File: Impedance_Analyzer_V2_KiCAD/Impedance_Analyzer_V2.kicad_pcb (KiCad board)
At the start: 2 copper layers, 94.4 x 90 mm, 87 parts, among them J1 Conn_Coaxial, J10 Conn_02x02_Counter_Clockwise, J11 Screw_Terminal_01x03, J12 Conn_02x02_Counter_Clockwise, J13 Conn_02x02_Counter_Clockwise, J14 Conn_02x02_Counter_Clockwise, J15 Conn_02x02_Counter_Clockwise, J16 Conn_02x02_Counter_Clockwise, J17 Conn_02x02_Counter_Clockwise, J2 Conn_Coaxial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

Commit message: Add STEP file, minor changes
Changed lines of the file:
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@@
     )
     (pad_to_mask_clearance 0)
-    (aux_axis_origin 70 142.5)
     (grid_origin 70 142.5)
     (pcbplotparams
@@
       (drillshape 0)
       (scaleselection 1)
-      (outputdirectory "Impedance Analyzer_V2RevA_Gerb/")
+      (outputdirectory "Impedance Analyzer_V2RevB_Gerb/")
     )
   )
@@
     (fp_line (start 1.6 -0.8) (end 1.6 0.8) (layer "F.Fab") (width 0.1))
     (fp_line (start 1.6 0.8) (end -1.6 0.8) (layer "F.Fab") (width 0.1))
-    (pad "1" smd roundrect locked (at -1.4625 0 180) (size 1.125 1.75) (layers "F.Cu" "F.Paste" "F.Mask") (roundrect_rratio 0.222222)
+    (pad "1" smd roundrect locked (at -1.4625 0 180) (size 1.125 1.75) (layers "F.Cu" "F.Paste" "F.Mask") (roundrect_rratio 0.2222222222)
       (net 57 "Net-(J17-Pad2)") (pintype "passive"))
-    (pad "2" smd roundrect locked (at 1.4625 0 180) (size 1.125 1.75) (layers "F.Cu" "F.Paste" "F.Mask") (roundrect_rratio 0.222222)
+    (pad "2" smd roundrect locked (at 1.4625 0 180) (size 1.125 1.75) (layers "F.Cu" "F.Paste" "F.Mask") (roundrect_rratio 0.2222222222)
       (net 8 "Net-(BUF1-Pad6)") (pintype "passive"))
     (model "${KICAD6_3DMODEL_DIR}/Resistor_SMD.3dshapes/R_1206_3216Metric.wrl"
@@
     (fp_line (start -1.6 0.8) (end -1.6 -0.8) (layer "F.Fab") (width 0.1))
     (fp_line (start 1.6 -0.8) (end 1.6 0.8) (layer "F.Fab") (width 0.1))
-    (pad "1" smd roundrect locked (at -1.4625 0) (size 1.125 1.75) (layers "F.Cu" "F.Paste" "F.Mask") (roundrect_rratio 0.222222)
+    (pad "1" smd roundrect locked (at -1.4625 0) (size 1.125 1.75) (layers "F.Cu" "F.Paste" "F.Mask") (roundrect_rratio 0.2222222222)
       (net 47 "Net-(R15-Pad1)") (pintype "passive"))
-    (pad "2" smd roundrect locked (at 1.4625 0) (size 1.125 1.75) (layers "F.Cu" "F.Paste" "F.Mask") (roundrect_rratio 0.222222)
+    (pad "2" smd roundrect locked (at 1.4625 0) (size 1.125 1.75) (layers "F.Cu" "F.Paste" "F.Mask") (roundrect_rratio 0.2222222222)
       (net 8 "Net-(BUF1-Pad6)") (pintype "passive"))
     (model "${KICAD6_3DMODEL_DIR}/Resistor_SMD.3dshapes/R_1206_3216Metric.wrl"
@@
     (fp_line (start -1.6 0.8) (end 1.6 0.8) (layer "B.Fab") (width 0.1))
     (fp_line (start 1.6 0.8) (end 1.6 -0.8) (layer "B.Fab") (width 0.1))
-    (pad "1" smd roundrect locked (at -1.5625 0 270) (size 1.325 1.8) (layers "B.Cu" "B.Paste" "B.Mask") (roundrect_rratio 0.188679)
+    (pad "1" smd roundrect locked (at -1.5625 0 270) (size 1.325 1.8) (layers "B.Cu" "B.Paste" "B.Mask") (roundrect_rratio 0.1886792453)
       (net 16 "+5VP") (pintype "passive"))
-    (pad "2" smd roundrect locked (at 1.5625 0 270) (size 1.325 1.8) (layers "B.Cu" "B.Paste" "B.Mask") (roundrect_rratio 0.188679)
+    (pad "2" smd roundrect locked (at 1.5625 0 270) (size 1.325 1.8) (layers "B.Cu" "B.Paste" "B.Mask") (roundrect_rratio 0.1886792453)
       (net 1 "GND") (pintype "passive"))
     (model "${KICAD6_3DMODEL_DIR}/Capacitor_SMD.3dshapes/C_1206_3216Metric.wrl"
@@
     (fp_line (start -1.6 0.8) (end 1.6 0.8) (layer "B.Fab") (width 0.1))
     (fp_line (start 1.6 0.8) (end 1.6 -0.8) (layer "B.Fab") (width 0.1))
-    (pad "1" smd roundrect locked (at -1.5625 0 270) (size 1.325 1.8) (layers "B.Cu" "B.Paste" "B.Mask") (roundrect_rratio 0.188679)
+    (pad "1" smd roundrect locked (at -1.5625 0 270) (size 1.325 1.8) (layers "B.Cu" "B.Paste" "B.Mask") (roundrect_rratio 0.1886792453)
       (net 1 "GND") (pintype "passive"))
-    (pad "2" smd roundrect locked (at 1.5625 0 270) (size 1.325 1.8) (layers "B.Cu" "B.Paste" "B.Mask") (roundrect_rratio 0.188679)
+    (pad "2" smd roundrect locked (at 1.5625 0 270) (size 1.325 1.8) (layers "B.Cu" "B.Paste" "B.Mask") (roundrect_rratio 0.1886792453)
       (net 15 "-5V") (pintype "passive"))
     (model "${KICAD6_3DMODEL_DIR}/Capacitor_SMD.3dshapes/C_1206_3216Metric.wrl"
@@
     (fp_line (start -1.6 0.8) (end 1.6 0.8) (layer "B.Fab") (width 0.1))
     (fp_line (start 1.6 0.8) (end 1.6 -0.8) (layer "B.Fab") (width 0.1))
-    (pad "1" smd roundrect locked (at -1.5625 0) (size 1.325 1.8) (layers "B.Cu" "B.Paste" "B.Mask") (roundrect_rratio 0.188679)
+    (pad "1" smd roundrect locked (at -1.5625 0) (size 1.325 1.8) (layers "B.Cu" "B.Paste" "B.Mask") (roundrect_rratio 0.1886792453)
       (net 16 "+5VP") (pintype "passive"))
-    (pad "2" smd roundrect locked (at 1.5625 0) (size 1.325 1.8) (layers "B.Cu" "B.Paste" "B.Mask") (roundrect_rratio 0.188679)
+    (pad "2" smd roundrect locked (at 1.5625 0) (size 1.325 1.8) (layers "B.Cu" "B.Paste" "B.Mask") (roundrect_rratio 0.1886792453)
       (net 1 "GND") (pintype "passive"))
     (model "${KICAD6_3DMODEL_DIR}/Capacitor_SMD.3dshapes/C_1206_3216Metric.wrl"
@@
     (fp_line (start -1.6 -0.8) (end -1.6 0.8) (layer "B.Fab") (width 0.1))
     (fp_line (start 1.6 0.8) (end 1.6 -0.8) (layer "B.Fab") (width 0.1))
-    (pad "1" smd roundrect locked (at -1.5625 0) (size 1.325 1.8) (layers "B.Cu" "B.Paste" "B.Mask") (roundrect_rratio 0.188679)
+    (pad "1" smd roundrect locked (at -1.5625 0) (size 1.325 1.8) (layers "B.Cu" "B.Paste" "B.Mask") (roundrect_rratio 0.1886792453)
       (net 1 "GND") (pintype "passive"))
-    (pad "2" smd roundrect locked (at 1.5625 0) (size 1.325 1.8) (layers "B.Cu" "B.Paste" "B.Mask") (roundrect_rratio 0.188679)
+    (pad "2" smd roundrect locked (at 1.5625 0) (size 1.325 1.8) (layers "B.Cu" "B.Paste" "B.Mask") (roundrect_rratio 0.1886792453)
       (net 15 "-5V") (pintype "passive"))
     (model "${KICAD6_3DMODEL_DIR}/Capacitor_SMD.3dshapes/C_1206_3216Metric.wrl"

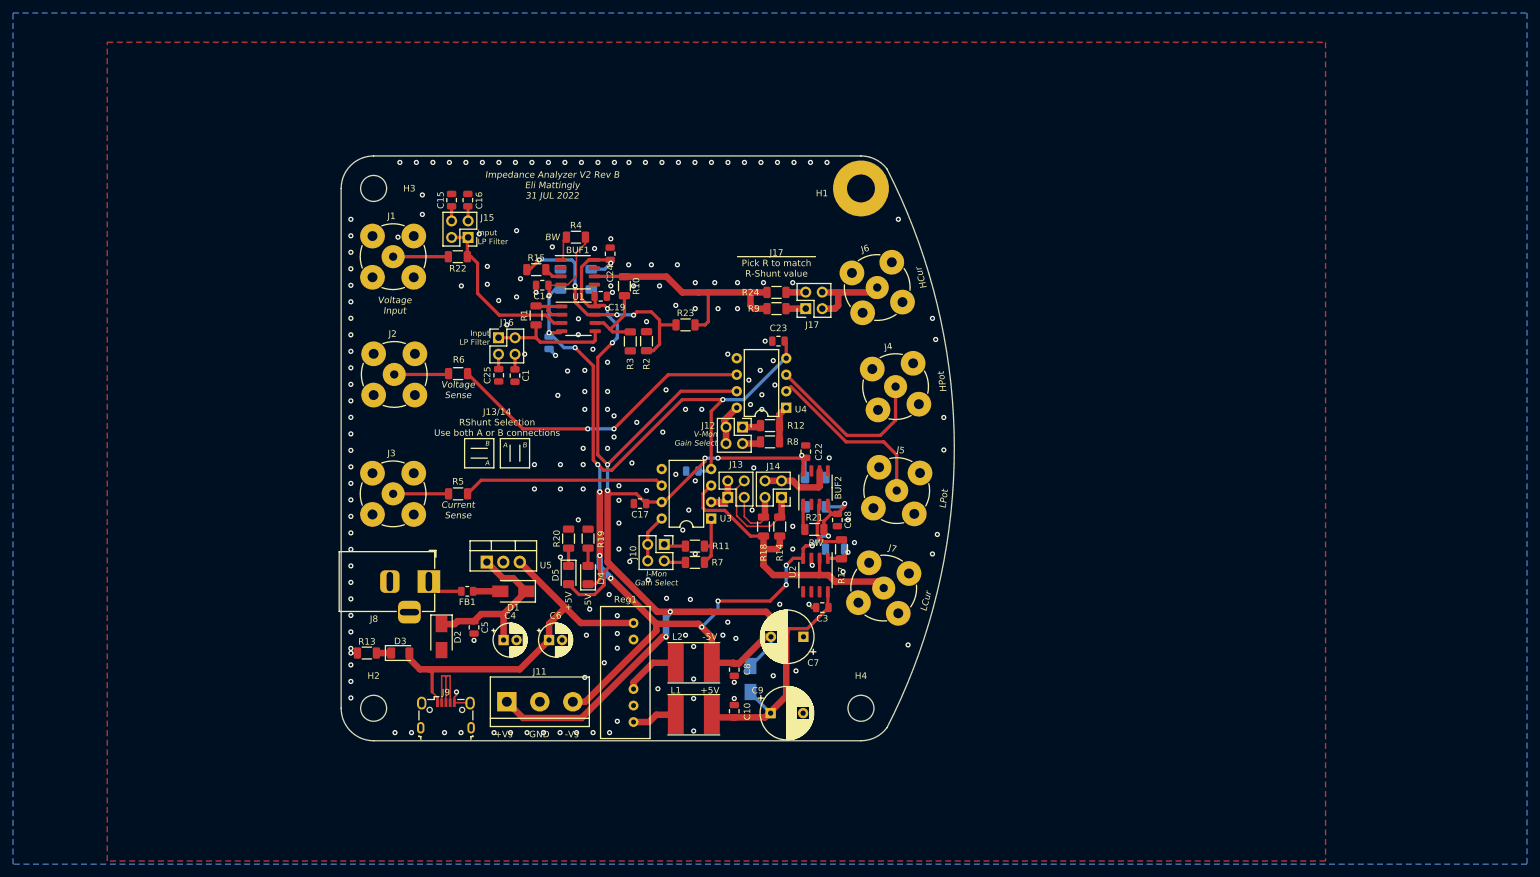
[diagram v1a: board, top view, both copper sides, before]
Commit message: Make Rev C + Curve tracer init
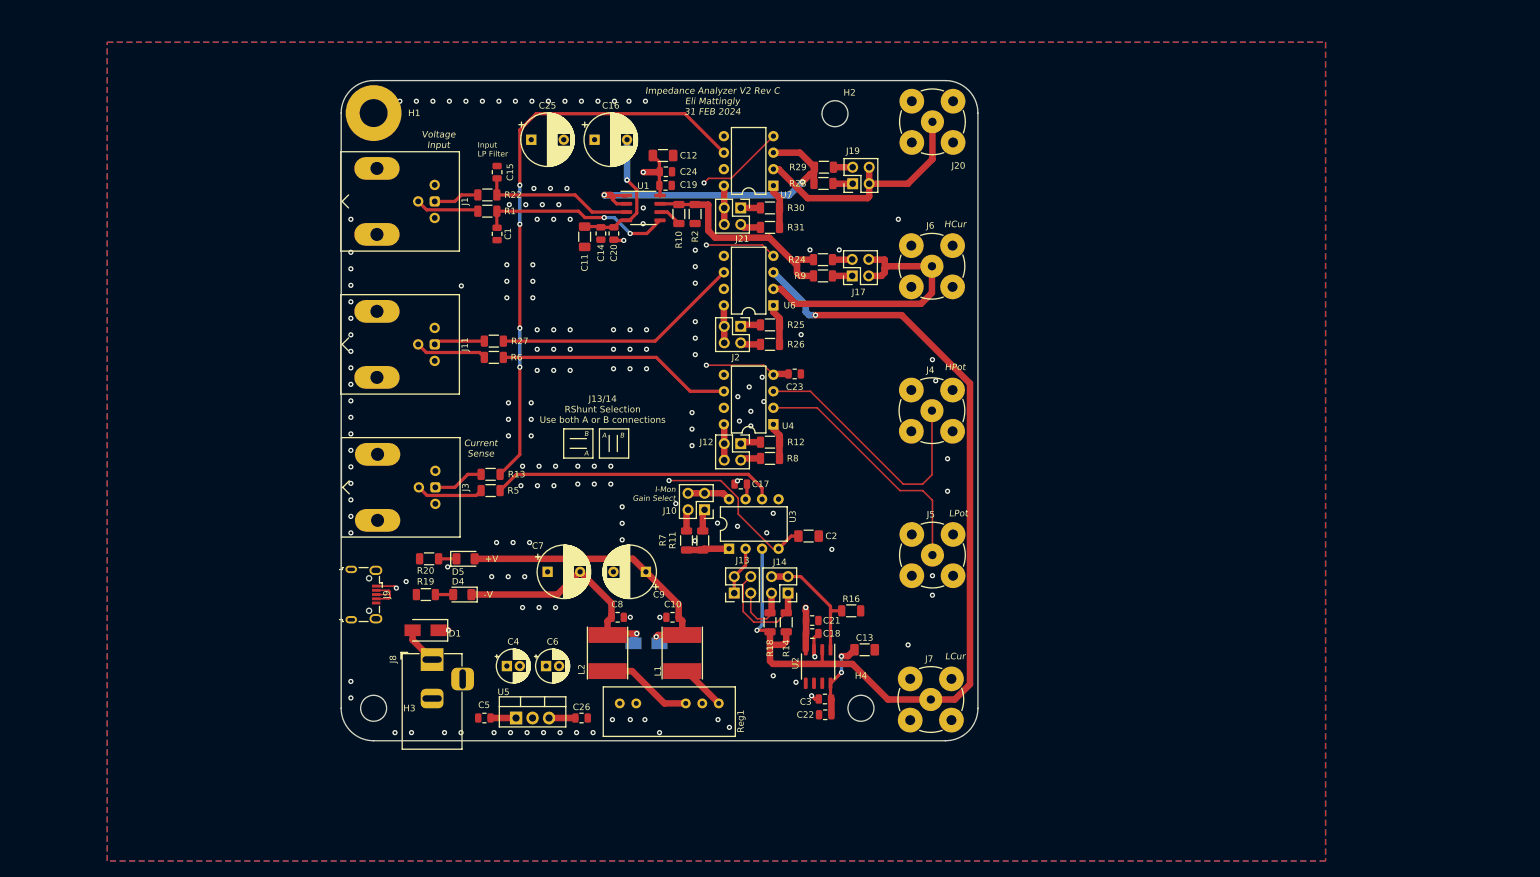
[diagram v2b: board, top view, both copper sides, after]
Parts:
- removed BUF1, BUF2: BUF634, Package_SO:SO-8_3.9x4.9mm_P1.27mm
- removed D2: D_TVS, Diode_SMD:D_SMA
- removed D3: LED, LED_SMD:LED_1206_3216Metric
- removed FB1: Ferrite_Bead, Resistor_SMD:R_0805_2012Metric
- removed J15, J16: Conn_02x02_Counter_Clockwise, Connector_PinHeader_2.54mm:PinHeader_2x02_P2.54mm_Vertical
- removed R15, R17: 50, Resistor_SMD:R_1206_3216Metric
- removed R21, R23, R3, R4: DNP, Resistor_SMD:R_1206_3216Metric
- added C26: 100n, Capacitor_SMD:C_0805_2012Metric, F.Cu at (107.0, 139.0)
- added J19: Conn_02x02_Counter_Clockwise, Connector_PinHeader_2.54mm:PinHeader_2x02_P2.54mm_Vertical, F.Cu at (148.7, 56.8)
- added J20: Conn_Coaxial, Connector_Coaxial:BNC_TEConnectivity_1478204_Vertical, F.Cu at (161.0, 47.2)
- added J21: Conn_02x02_Counter_Clockwise, Connector_PinHeader_2.54mm:PinHeader_2x02_P2.54mm_Vertical, F.Cu at (131.5, 60.5)
- added R25: 1k, Resistor_SMD:R_1206_3216Metric, F.Cu at (136.0, 78.5)
- added R26: 10k, Resistor_SMD:R_1206_3216Metric, F.Cu at (136.0, 81.5)
- added R27: 47, Resistor_SMD:R_1206_3216Metric, F.Cu at (93.5, 81.0)
- added R28: 1k, Resistor_SMD:R_1206_3216Metric, F.Cu at (144.2, 56.7)
- added R29: 10k, Resistor_SMD:R_1206_3216Metric, F.Cu at (144.3, 54.2)
- added R30: 1k, Resistor_SMD:R_1206_3216Metric, F.Cu at (136.0, 60.5)
- added R31: 10k, Resistor_SMD:R_1206_3216Metric, F.Cu at (136.0, 63.5)
- added U6: INA129, Package_DIP:DIP-8_W7.62mm, F.Cu at (136.5, 75.5)
- added U7: INA129, Package_DIP:DIP-8_W7.62mm, F.Cu at (136.5, 57.1)
- C11, C12, C13, C2, C20, C21, R16: moved to F.Cu
- C15: value 1n -> 10n
- C16, C25: value 10n -> CP; footprint Capacitor_SMD:C_0805_2012Metric -> Capacitor_THT:CP_Radial_D8.0mm_P5.00mm
- J1, J3: value Conn_Coaxial -> Conn_Coaxial_x2; footprint Connector_Coaxial:BNC_TEConnectivity_1478204_Vertical -> Connector_Coaxial:BNC_Win_364A2x95_Horizontal
- J11: value Screw_Terminal_01x03 -> Conn_Coaxial_x2; footprint TerminalBlock:TerminalBlock_bornier-3_P5.08mm -> Connector_Coaxial:BNC_Win_364A2x95_Horizontal
- J2: value Conn_Coaxial -> Conn_02x02_Counter_Clockwise; footprint Connector_Coaxial:BNC_TEConnectivity_1478204_Vertical -> Connector_PinHeader_2.54mm:PinHeader_2x02_P2.54mm_Vertical
- R13: value 1k -> 47
- U1, U2: value LM358 -> AD8022
- moved H2 115.8 mm to (146.0, 46.0)
- moved H3 80.0 mm to (75.0, 137.5)
- moved H1 75.9 mm to (75.0, 45.9)
- moved J11 56.1 mm to (84.4, 81.5), turned to 90 degrees
- moved J2 53.8 mm to (131.5, 78.7), turned to -90 degrees
- moved C7 40.6 mm to (101.8, 116.5), turned to 0 degrees
- moved C22 40.6 mm to (144.5, 138.5), turned to 180 degrees
- moved C25 36.6 mm to (99.3, 50.0), turned to 0 degrees
- moved R13 33.4 mm to (93.0, 101.5)
- moved C21 29.5 mm to (142.5, 124.0), turned to 0 degrees
- moved C9 29.0 mm to (116.9, 116.5), turned to 180 degrees
- moved C13 27.6 mm to (150.6, 128.5)
- moved R19 26.4 mm to (83.0, 120.0), turned to 180 degrees
- moved U5 24.4 mm to (96.9, 139.0)
- moved J9 22.4 mm to (73.5, 120.0), turned to -90 degrees
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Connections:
- C1 pad 1: Net-(C1-Pad1) -> Net-(R1-Pad1)
- C15 pad 1: Net-(C15-Pad1) -> Net-(R22-Pad1)
- C16 pad 1: Net-(C16-Pad1) -> GND
- C16 pad 2: GND -> -5V
- C25 pad 1: Net-(C25-Pad1) -> +5VP
- D1 pad 2: Net-(D1-Pad2) -> Net-(J8-Pad1)
- J1 pad 1: InputSig -> BaseGateSig
- J1 pad 2: GND -> InputSig
- J11 pad 1: +5VP -> Net-(J11-Pad1)
- J11 pad 2: GND -> Net-(R6-Pad2)
- J11 pad 3: -5V -> GND
- J14 pad 3: Net-(BUF2-Pad6) -> Net-(R16-Pad1)
- J14 pad 4: Net-(BUF2-Pad6) -> Net-(R16-Pad1)
- J2 pad 2: GND -> Net-(J2-Pad2)
- J3 pad 2: GND -> Net-(J3-Pad2)
- J8 pad 1: Net-(FB1-Pad2) -> Net-(J8-Pad1)
- R1 pad 1: Net-(J16-Pad1) -> Net-(R1-Pad1)
- R1 pad 2: Net-(R1-Pad2) -> InputSig
- R10 pad 1: Net-(BUF1-Pad6) -> Net-(R10-Pad1)
- R13 pad 1: Net-(D3-Pad1) -> BaseIMon
- R13 pad 2: GND -> Net-(J3-Pad1)
- R2 pad 1: Net-(R15-Pad1) -> Net-(R10-Pad1)
- R22 pad 1: Net-(J15-Pad1) -> Net-(R22-Pad1)
- R22 pad 2: InputSig -> BaseGateSig
- R24 pad 2: Net-(BUF1-Pad6) -> Net-(R10-Pad1)
- R5 pad 2: Net-(J3-Pad1) -> Net-(J3-Pad2)
- R6 pad 2: Net-(J2-Pad1) -> Net-(R6-Pad2)
- R9 pad 2: Net-(BUF1-Pad6) -> Net-(R10-Pad1)
- U1 pad 1: Net-(R1-Pad2) -> Net-(R28-Pad2)
- U1 pad 2: Net-(R1-Pad2) -> Net-(R28-Pad2)
- U1 pad 3: Net-(J15-Pad1) -> Net-(R22-Pad1)
- U1 pad 5: Net-(J16-Pad1) -> Net-(R1-Pad1)
- U1 pad 7: Net-(R15-Pad1) -> Net-(R10-Pad1)
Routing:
- net IMon+: track 47.5 -> 144.4 mm, vias 0 -> 2
- net BaseIMon: track 0.00 -> 89.2 mm, vias 0 -> 4
- net Net-(R28-Pad2): track 0.00 -> 50.0 mm, vias 0 -> 2
- net Net-(BUF1-Pad6): track 39.1 -> 0.00 mm
- net Net-(R27-Pad1): track 0.00 -> 38.3 mm
- net BaseGateOutput: track 0.00 -> 38.2 mm
- net Net-(R15-Pad1): track 37.5 -> 0.00 mm, vias 4 -> 0
- net Net-(R10-Pad1): track 0.00 -> 34.6 mm
- net +5VP: track 241.6 -> 209.1 mm, vias 10 -> 4
- net Net-(R1-Pad1): track 0.00 -> 29.9 mm, vias 0 -> 2
- net IOut: track 14.9 -> 44.7 mm
- net Net-(J15-Pad1): track 26.7 -> 0.00 mm
- net Net-(R22-Pad1): track 0.00 -> 23.6 mm
- net Net-(J16-Pad1): track 18.7 -> 0.00 mm
- net Net-(R16-Pad1): track 4.30 -> 19.5 mm, vias 1 -> 0
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- added copper zone on In1.Cu, net GND
- added copper zone on In2.Cu, net GND
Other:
- board size 94.4 x 90 mm -> 98 x 101.6 mm
- copper layers 2 -> 4
- board text added: "+V"
- board text added: "-V"
- board text added: "Impedance Analyzer V2 Rev C Eli Mattingly 31 FEB 2024"
- board text removed: "+5V"
- board text removed: "+Vs"
- board text removed: "-5V"
- board text removed: "-Vs"
- board text removed: "BW"
- board text removed: "GND"
- board text removed: "Impedance Analyzer V2 Rev B Eli Mattingly 31 JUL 2022"
- board text removed: "J17 Pick R to match R-Shunt value"
- board text removed: "V-Mon Gain Select"
- board text removed: "Voltage Sense"

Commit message: Update Impedance board
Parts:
- added J15: Conn_01x02_Male, Connector_PinHeader_2.54mm:PinHeader_1x02_P2.54mm_Horizontal, F.Cu at (166.9, 78.5)
- added J16: Conn_01x02_Male, Connector_PinHeader_2.54mm:PinHeader_1x02_P2.54mm_Horizontal, F.Cu at (166.9, 100.5)
- added J18: Conn_01x02_Male, Connector_PinHeader_2.54mm:PinHeader_1x02_P2.54mm_Horizontal, F.Cu at (166.5, 122.7)
- J20, J4, J5, J6, J7: footprint Connector_Coaxial:BNC_TEConnectivity_1478204_Vertical -> Eli_Lib:31-5486-1010 BNC Panel RA
- moved J4 1.00 mm to (160.9, 90.7), turned to -90 degrees
- moved J5 1.00 mm to (161.0, 112.9), turned to -90 degrees
- moved J6 1.00 mm to (160.9, 68.5), turned to -90 degrees
- moved J7 1.00 mm to (160.8, 135.2), turned to -90 degrees
- moved J20 0.70 mm to (161.0, 48.0), turned to -90 degrees
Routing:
- net Net-(J15-Pad2): track 40.8 -> 63.4 mm, vias 0 -> 2
- net Net-(J5-Pad1): track 38.8 -> 59.7 mm, vias 0 -> 2
- net IOut: track 44.7 -> 54.6 mm
- net IMon+: track 144.4 -> 142.1 mm
- net BaseGateOutput: track 38.2 -> 37.5 mm
- net GND: vias 165 -> 163
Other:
- outline, holes or cut-outs redrawn
